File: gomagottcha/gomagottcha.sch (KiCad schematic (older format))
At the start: 16 parts

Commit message: updated schematic
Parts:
- added C? (x4): 10uF, symbol tama-sym:C
- added C? (x2): 0.1uF, symbol tama-sym:C
- added R? (x4): 10k, symbol Device:R
- added R?: 11k, symbol Device:R
- added R?: 40k2, symbol Device:R
- added SW?: SW_DIP_x01, symbol tama-sym:SW_DIP_x01
- added U? (x2): VMotor1670-1000-ND, symbol tama-sym:VMotor1670-1000-ND
- added U?N, U?N? (x2), U?P, U?P? (x2): MOSNP, symbol tama-sym:MOSNP
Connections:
- wire segments 47 -> 90
- no-connect marks 19 -> 20

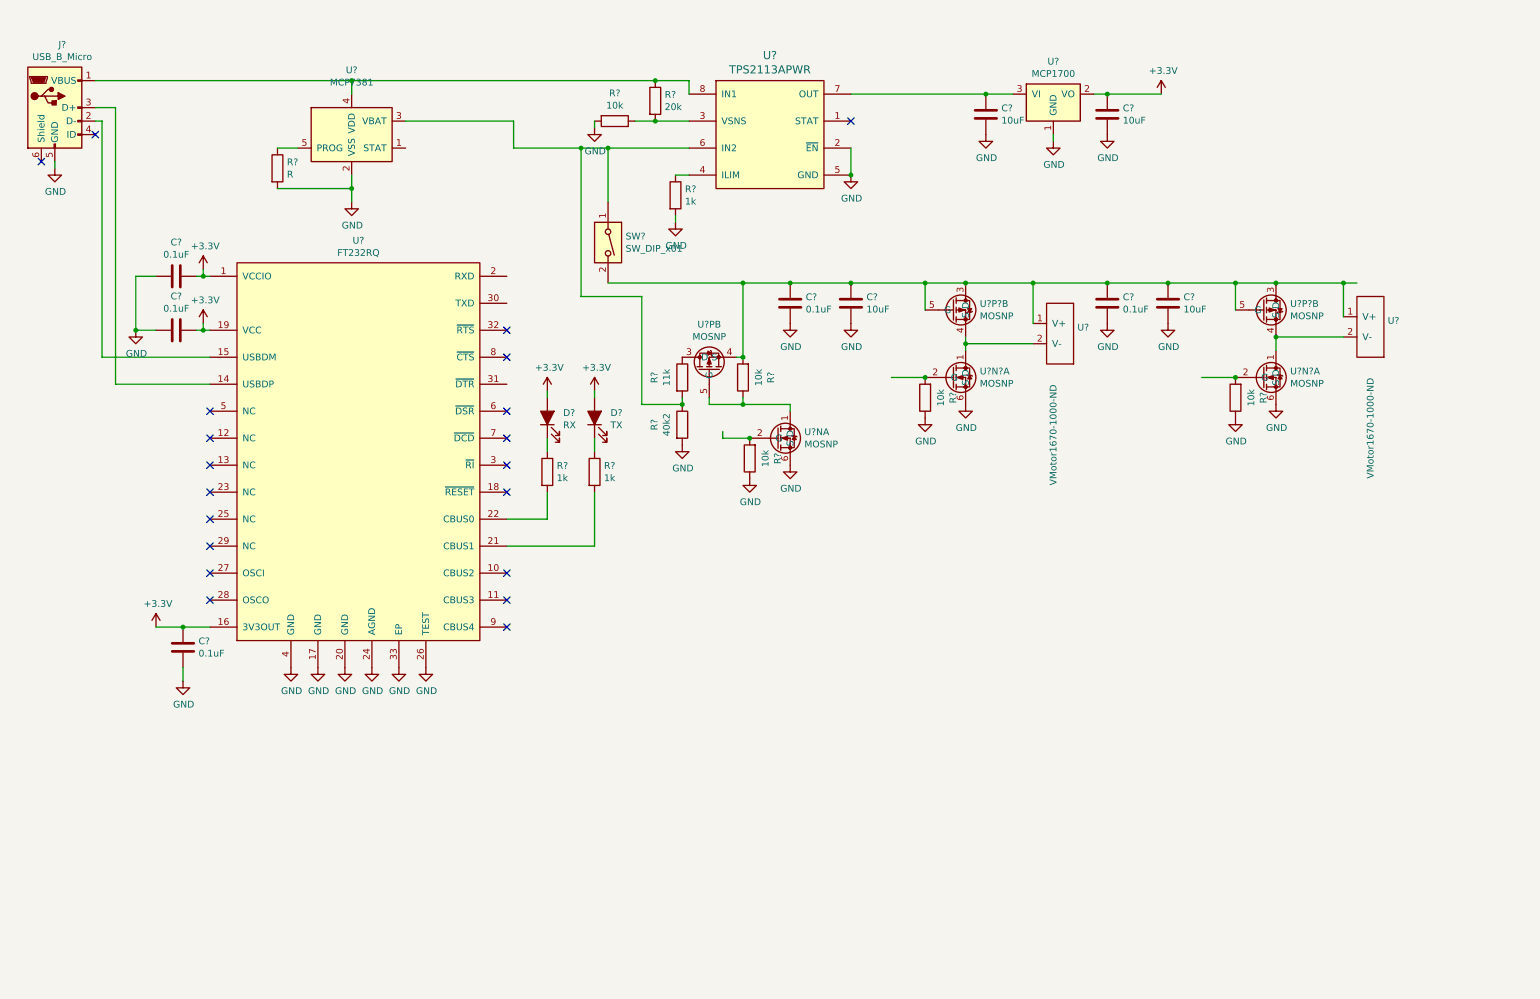
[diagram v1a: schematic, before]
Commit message: LCD and IMU hooked up
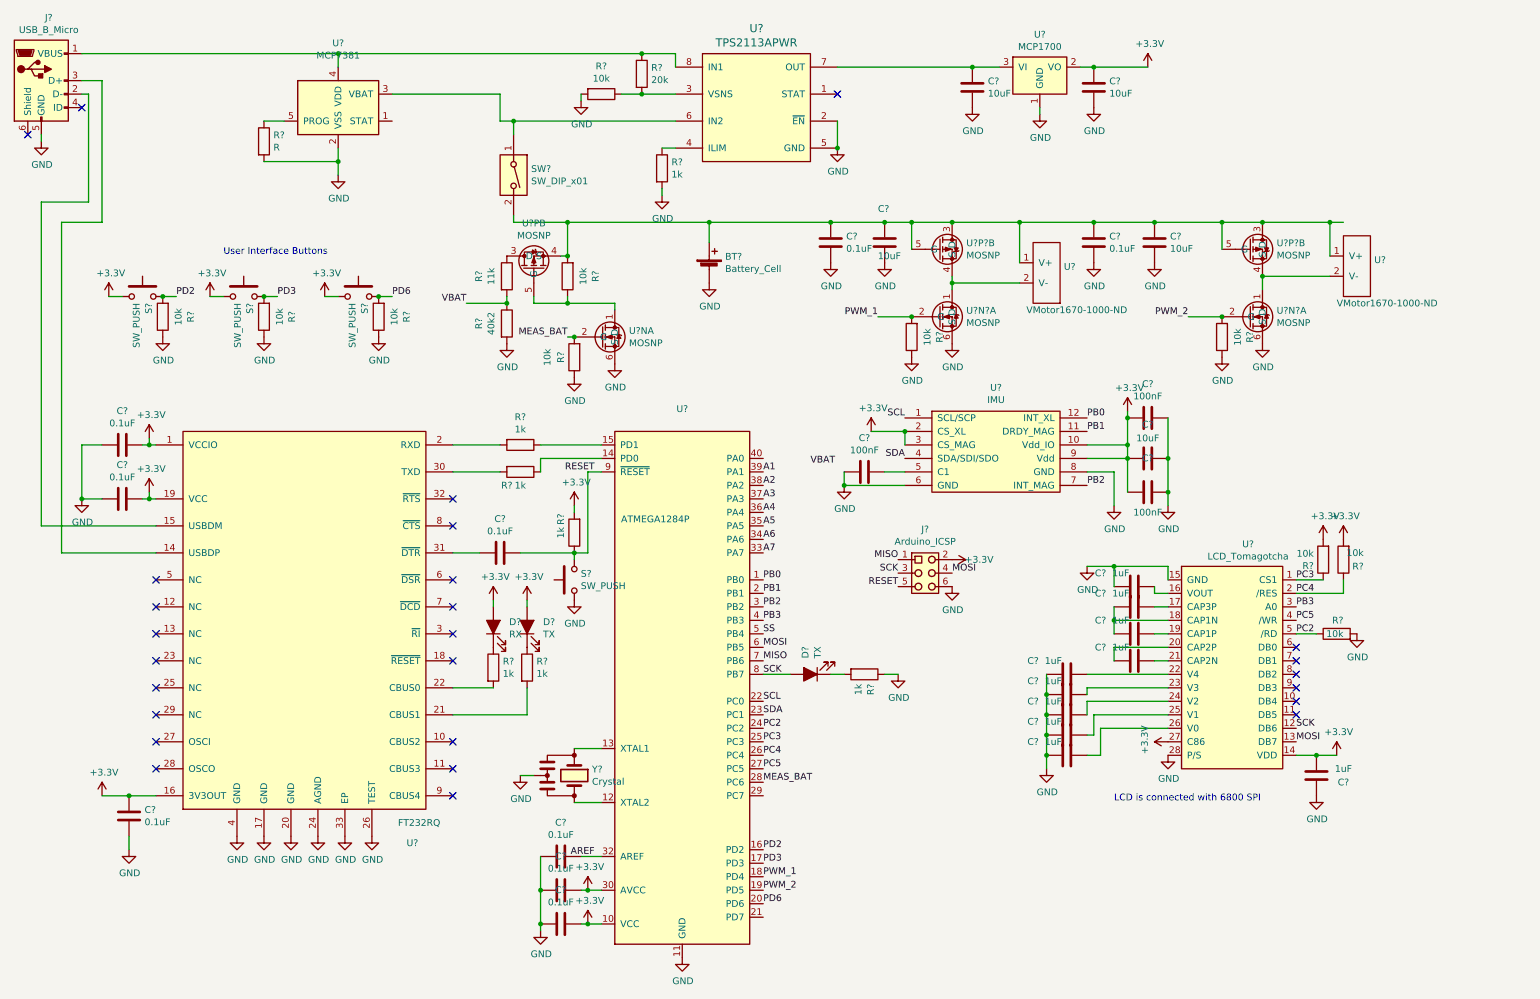
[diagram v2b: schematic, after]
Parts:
- added BT?: Battery_Cell, symbol Device:Battery_Cell
- added C? (x4): 0.1uF, symbol tama-sym:C
- added C?: 10uF, symbol tama-sym:C
- added C? (x3): 100nF, symbol tama-sym:C
- added C? (x10): 1uF, symbol tama-sym:C
- added D?: TX, symbol tama-sym:LED_ALT
- added J?: Arduino_ICSP, symbol tama-sym:Arduino_ICSP
- added R? (x4): 1k, symbol Device:R
- added R? (x6): 10k, symbol Device:R
- added S? (x4): SW_PUSH, symbol tama-sym:SW_PUSH
- added U?: ATMEGA1284P, symbol tama-sym:ATMEGA1284P
- added U?: LCD_Tomagotcha, symbol tama-sym:LCD_Tomagotcha
- added U?: IMU, symbol tama-sym:IMU
- added Y?: Crystal, symbol tama-sym:Crystal
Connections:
- net labels added: A1, A2, A3, A4, A5, A6, A7, AREF, MEAS_BAT, MISO, MOSI, PB0, PB1, PB2, PB3, PC2, PC3, PC4, PC5, PD2, PD3, PD6, PWM_1, PWM_2, RESET, SCK, SCL, SDA, SS, VBAT
- wire segments 90 -> 173
- no-connect marks 20 -> 26
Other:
- note added: "LCD is connected with 6800 SPI"
- note added: "User Interface Buttons"
- moved on the sheet: C?, D?, J?, R?, SW?, U?, U?N?A, U?NA, U?P?B, U?PB

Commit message: Add some footprints to symbols
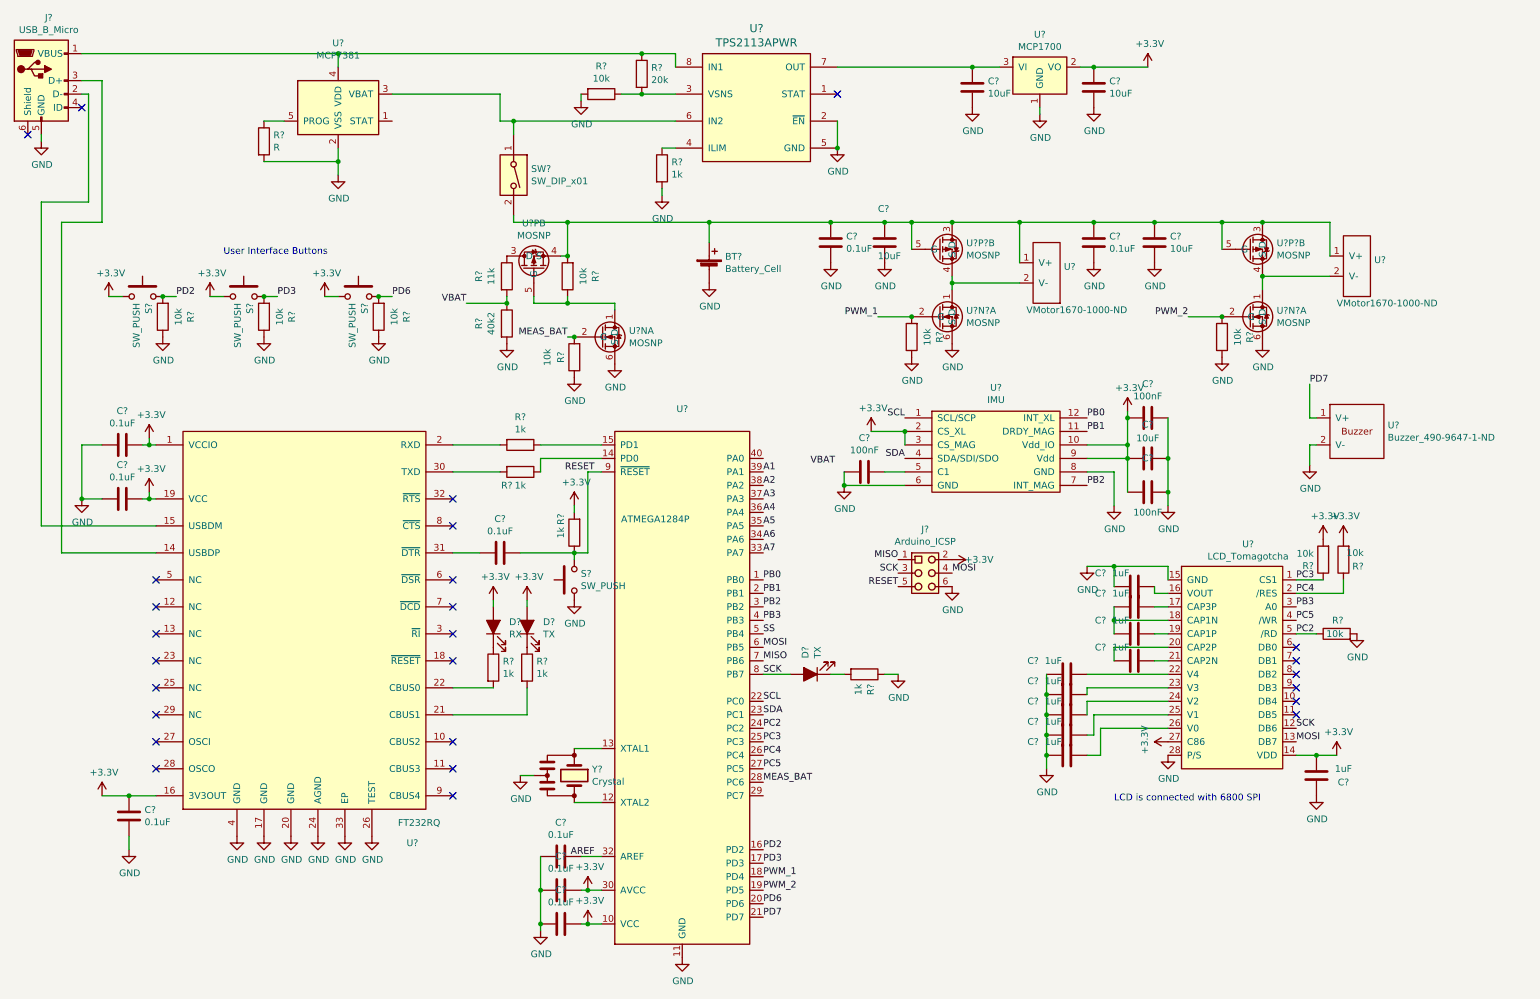
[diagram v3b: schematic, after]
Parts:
- added U?: Buzzer_490-9647-1-ND, tama-footprints:Buzzer 490-9647-1-ND, symbol tama-sym:Buzzer_490-9647-1-ND
- U?: footprint (none) -> Package_SO:TSSOP-28_4.4x9.7mm_P0.65mm
- U?: footprint (none) -> tama-footprints:TQFP-44_10x10mm_P0.8mm
- U?: footprint (none) -> tama-footprints:LCD NHD-C12864LZ-FSW-FBW-3V3-ND
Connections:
- net GND: now also U?.2 (V-)
- net PD7: now reaches U?.21 (PD7)
- net PD7: now also U?.1 (V+)
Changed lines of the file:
@@
 F 0 "U?" H 3550 3350 50  0000 C CNN
 F 1 "FT232RQ" H 3600 3500 50  0000 C CNN
-F 2 "" H 2750 5950 50  0001 C CNN
+F 2 "Package_SO:TSSOP-28_4.4x9.7mm_P0.65mm" H 2750 5950 50  0001 C CNN
 F 3 "" H 2750 5950 50  0001 C CNN
 	1    2750 5000
@@
 Wire Wire Line
 	10350 2300 10350 2050
-Connection ~ 10350 2050
-Wire Wire Line
-	10350 2050 10450 2050
 $Comp
 L tama-sym:C C?
@@
 F 0 "U?" H 5550 7067 50  0000 C CNN
 F 1 "ATMEGA1284P" H 5350 6250 50  0000 C CNN
-F 2 "" H 4750 4700 50  0001 C CNN
+F 2 "tama-footprints:TQFP-44_10x10mm_P0.8mm" H 4750 4700 50  0001 C CNN
 F 3 "" H 4750 4700 50  0001 C CNN
 	1    5550 5250
@@
 F 0 "U?" H 9743 8065 50  0000 C CNN
 F 1 "LCD_Tomagotcha" H 9743 7974 50  0000 C CNN
-F 2 "" H 9600 6200 50  0001 C CNN
+F 2 "tama-footprints:LCD NHD-C12864LZ-FSW-FBW-3V3-ND" H 9600 6200 50  0001 C CNN
 F 3 "" H 9600 6200 50  0001 C CNN
 	1    9650 6250
@@
 Text Notes 2150 2300 0    50   ~ 0
 User Interface Buttons
+$Comp
+L tama-sym:Buzzer_490-9647-1-ND U?
+U 1 1 5CA808E8
+P 10550 3850
+F 0 "U?" H 10778 4146 50  0000 L CNN
+F 1 "Buzzer_490-9647-1-ND" H 10778 4055 50  0000 L CNN
+F 2 "tama-footprints:Buzzer 490-9647-1-ND" H 10550 3800 50  0001 C CNN
+F 3 "" H 10550 3800 50  0001 C CNN
+	1    10550 3850
+	1    0    0    -1
+$EndComp
+$Comp
+L power:GND #PWR?
+U 1 1 5CA809E9
+P 10200 3850
+F 0 "#PWR?" H 10200 3600 50  0001 C CNN
+F 1 "GND" H 10205 3677 50  0000 C CNN
+F 2 "" H 10200 3850 50  0001 C CNN
+F 3 "" H 10200 3850 50  0001 C CNN
+	1    10200 3850
+	1    0    0    -1
+$EndComp
+Wire Wire Line
+	10250 3700 10200 3700
+Wire Wire Line
+	10200 3700 10200 3850
+Text Label 6150 7200 0    50   ~ 0
+PD7
+Text Label 10200 3250 0    50   ~ 0
+PD7
+Wire Wire Line
+	10200 3250 10200 3500
+Wire Wire Line
+	10200 3500 10250 3500
 $EndSCHEMATC

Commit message: Add more footprints to schematic
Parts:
- J?: footprint (none) -> tama-footprints:USB micro 609-4616-1-ND
- U?: footprint (none) -> Package_TO_SOT_SMD:SOT-23-5
- U?: footprint (none) -> Package_TO_SOT_SMD:SOT-23
- U?: footprint (none) -> Package_SO:TSSOP-8_4.4x3mm_P0.65mm
- U? (x2): footprint (none) -> tama-footprints:VMotor 1670-1000-ND
- U?: footprint tama-footprints:TQFP-44_10x10mm_P0.8mm -> (none)
- U?: footprint (none) -> tama-footprints:IMU
- U?N, U?N? (x2), U?P, U?P? (x2): footprint (none) -> tama-footprints:SOT-363_SC-70-6
- Y?: footprint (none) -> tama-footprints:8MHz_Crystal
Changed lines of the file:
@@
 F 0 "J?" H 855 1467 50  0000 C CNN
 F 1 "USB_B_Micro" H 855 1376 50  0000 C CNN
-F 2 "" H 950 950 50  0001 C CNN
+F 2 "tama-footprints:USB micro 609-4616-1-ND" H 950 950 50  0001 C CNN
 F 3 "~" H 950 950 50  0001 C CNN
 	1    800  1000
@@
 F 0 "U?" H 3000 1878 50  0000 C CNN
 F 1 "MCP7381" H 3000 1787 50  0000 C CNN
-F 2 "" H 2700 1800 50  0001 C CNN
+F 2 "Package_TO_SOT_SMD:SOT-23-5" H 2700 1800 50  0001 C CNN
 F 3 "" H 2700 1800 50  0001 C CNN
 	1    3000 1300
@@
 F 0 "U?" H 8200 1142 50  0000 C CNN
 F 1 "MCP1700" H 8200 1051 50  0000 C CNN
-F 2 "" H 8200 900 50  0001 C CNN
+F 2 "Package_TO_SOT_SMD:SOT-23" H 8200 900 50  0001 C CNN
 F 3 "" H 8200 900 50  0001 C CNN
 	1    8200 900
@@
 F 0 "U?" H 6100 1787 60  0000 C CNN
 F 1 "TPS2113APWR" H 6100 1681 60  0000 C CNN
-F 2 "" H 6100 1350 60  0001 C CNN
+F 2 "Package_SO:TSSOP-8_4.4x3mm_P0.65mm" H 6100 1350 60  0001 C CNN
 F 3 "" H 6100 1350 60  0001 C CNN
 	1    6100 1200
@@
 F 0 "U?N" H 5155 2946 50  0000 L CNN
 F 1 "MOSNP" H 5155 2855 50  0000 L CNN
-F 2 "" H 5000 2900 50  0001 C CNN
+F 2 "tama-footprints:SOT-363_SC-70-6" H 5000 2900 50  0001 C CNN
 F 3 "" H 5000 2900 50  0001 C CNN
 	1    5050 2900
@@
 F 0 "U?P" V 4693 2300 50  0000 C CNN
 F 1 "MOSNP" V 4602 2300 50  0000 C CNN
-F 2 "" H 4400 2300 50  0001 C CNN
+F 2 "tama-footprints:SOT-363_SC-70-6" H 4400 2300 50  0001 C CNN
 F 3 "" H 4400 2300 50  0001 C CNN
 	2    4450 2300
@@
 F 0 "U?P?" H 7655 2296 50  0000 L CNN
 F 1 "MOSNP" H 7655 2205 50  0000 L CNN
-F 2 "" H 7500 2250 50  0001 C CNN
+F 2 "tama-footprints:SOT-363_SC-70-6" H 7500 2250 50  0001 C CNN
 F 3 "" H 7500 2250 50  0001 C CNN
 	2    7550 2250
@@
 F 0 "U?P?" H 9955 2296 50  0000 L CNN
 F 1 "MOSNP" H 9955 2205 50  0000 L CNN
-F 2 "" H 9800 2250 50  0001 C CNN
+F 2 "tama-footprints:SOT-363_SC-70-6" H 9800 2250 50  0001 C CNN
 F 3 "" H 9800 2250 50  0001 C CNN
 	2    9850 2250
@@
 F 0 "U?N?" H 7655 2796 50  0000 L CNN
 F 1 "MOSNP" H 7655 2705 50  0000 L CNN
-F 2 "" H 7500 2750 50  0001 C CNN
+F 2 "tama-footprints:SOT-363_SC-70-6" H 7500 2750 50  0001 C CNN
 F 3 "" H 7500 2750 50  0001 C CNN
 	1    7550 2750
@@
 F 0 "U?N?" H 9955 2796 50  0000 L CNN
 F 1 "MOSNP" H 9955 2705 50  0000 L CNN
-F 2 "" H 9800 2750 50  0001 C CNN
+F 2 "tama-footprints:SOT-363_SC-70-6" H 9800 2750 50  0001 C CNN
 F 3 "" H 9800 2750 50  0001 C CNN
 	1    9850 2750
@@
 F 0 "U?" H 8378 3121 50  0000 L CNN
 F 1 "VMotor1670-1000-ND" H 8100 2800 50  0000 L CNN
-F 2 "" H 8250 2750 50  0001 C CNN
+F 2 "tama-footprints:VMotor 1670-1000-ND" H 8250 2750 50  0001 C CNN
 F 3 "" H 8250 2750 50  0001 C CNN
 	1    8250 2750
@@
 F 0 "U?" H 10678 3071 50  0000 L CNN
 F 1 "VMotor1670-1000-ND" H 10400 2750 50  0000 L CNN
-F 2 "" H 10550 2700 50  0001 C CNN
+F 2 "tama-footprints:VMotor 1670-1000-ND" H 10550 2700 50  0001 C CNN
 F 3 "" H 10550 2700 50  0001 C CNN
 	1    10550 2700
@@
 F 0 "U?" H 5550 7067 50  0000 C CNN
 F 1 "ATMEGA1284P" H 5350 6250 50  0000 C CNN
-F 2 "tama-footprints:TQFP-44_10x10mm_P0.8mm" H 4750 4700 50  0001 C CNN
+F 2 "" H 4750 4700 50  0001 C CNN
 F 3 "" H 4750 4700 50  0001 C CNN
 	1    5550 5250
@@
 F 0 "Y?" V 4704 6281 50  0000 L CNN
 F 1 "Crystal" V 4795 6281 50  0000 L CNN
-F 2 "" H 4750 6150 50  0001 C CNN
+F 2 "tama-footprints:8MHz_Crystal" H 4750 6150 50  0001 C CNN
 F 3 "~" H 4750 6150 50  0001 C CNN
 	1    4750 6150
@@
 F 0 "U?" H 7875 4825 50  0000 C CNN
 F 1 "IMU" H 7875 4734 50  0000 C CNN
-F 2 "" H 7400 4050 50  0001 C CNN
+F 2 "tama-footprints:IMU" H 7400 4050 50  0001 C CNN
 F 3 "" H 7400 4050 50  0001 C CNN
 	1    7400 4050
